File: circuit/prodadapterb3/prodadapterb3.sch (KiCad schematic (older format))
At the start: 8 parts, among them J1 Conn_02x20_Odd_Even, J2 Conn_02x05_Odd_Even, J3 Conn_01x02, J4 Conn_02x20_Odd_Even, U1 24LC128

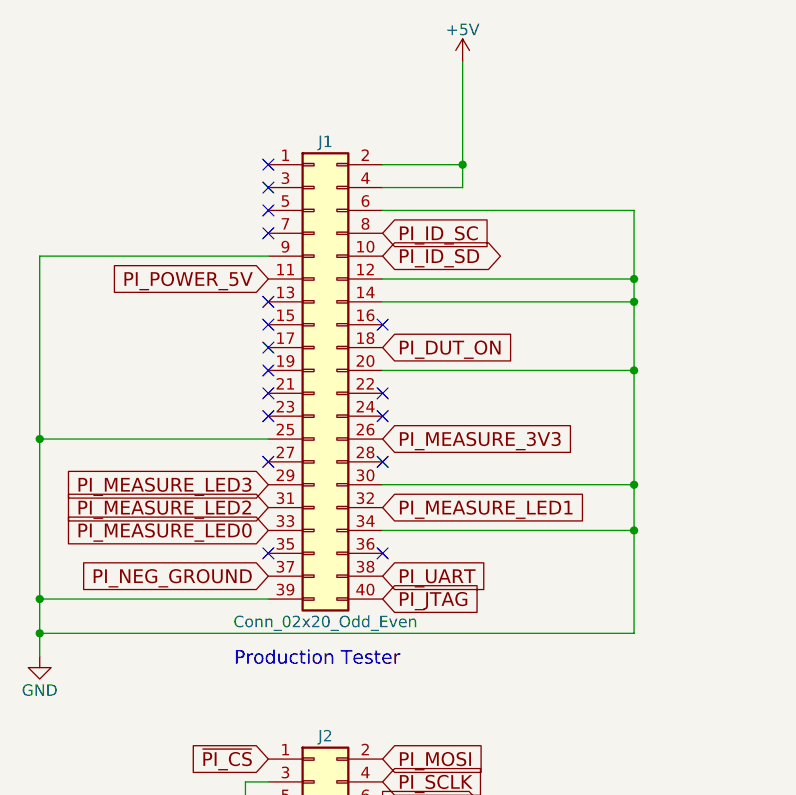
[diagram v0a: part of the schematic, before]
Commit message: prodadapterb3: move resistors out of the way and connect up 3v3 line
Signed-off-by: Gavan Fantom <gavan.fantom@unipart.io>
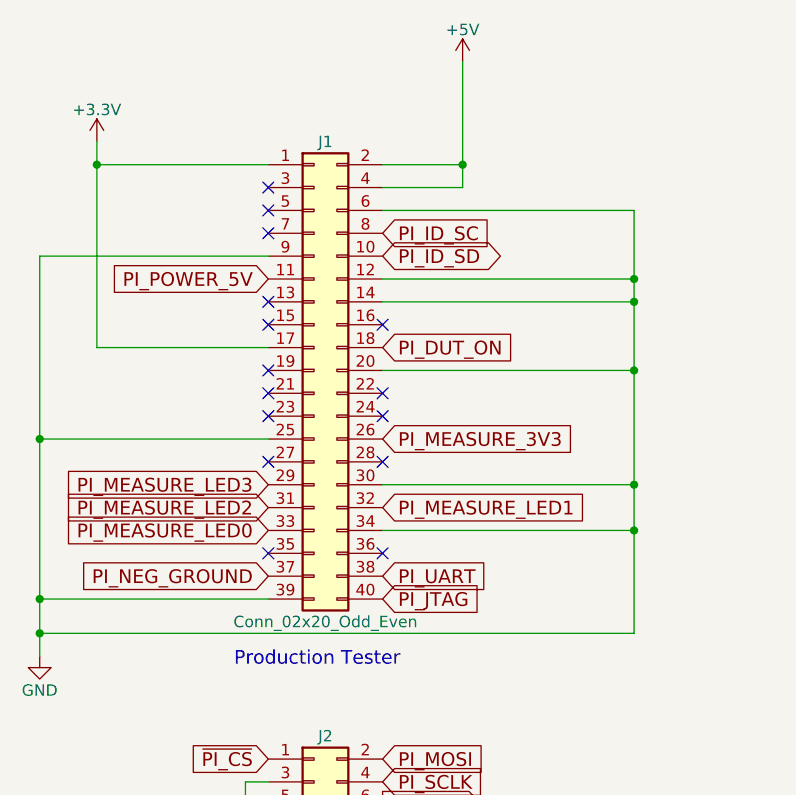
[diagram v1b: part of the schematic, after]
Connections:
- net +3V3: now also J1.1 (Pin_1), J1.17 (Pin_17)
- no-connect marks 27 -> 25
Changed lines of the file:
@@
 $EndComp
 Wire Wire Line
-	2900 3800 1900 3800
+	1900 3800 2900 3800
 Wire Wire Line
 	1900 2300 1900 4050
@@
 Connection ~ 1900 3100
 Wire Wire Line
-	1900 3950 4500 3950
+	4500 3950 1900 3950
 Wire Wire Line
-	4500 3950 4500 2100
+	4500 2100 4500 3950
 Wire Wire Line
 	4500 2100 3400 2100
@@
 	1    0    0    -1
 $EndComp
-NoConn ~ 2900 1900
 NoConn ~ 2900 2000
 NoConn ~ 2900 2100
@@
 NoConn ~ 2900 2600
 NoConn ~ 2900 2500
-NoConn ~ 2900 2700
 NoConn ~ 6500 2200
 NoConn ~ 7000 2200
@@
 Connection ~ 6250 1900
 Connection ~ 7100 1900
+Wire Wire Line
+	2150 2700 2900 2700
+Wire Wire Line
+	2150 1800 2150 2700
+Wire Wire Line
+	2150 1900 2900 1900
+Connection ~ 2150 1900
+$Comp
+L +3.3V #PWR011
+U 1 1 5DC1768B
+P 2150 1800
+F 0 "#PWR011" H 2150 1650 50  0001 C CNN
+F 1 "+3.3V" H 2150 1940 50  0000 C CNN
+F 2 "" H 2150 1800 50  0001 C CNN
+F 3 "" H 2150 1800 50  0001 C CNN
+	1    2150 1800
+	1    0    0    -1
+$EndComp
 $EndSCHEMATC

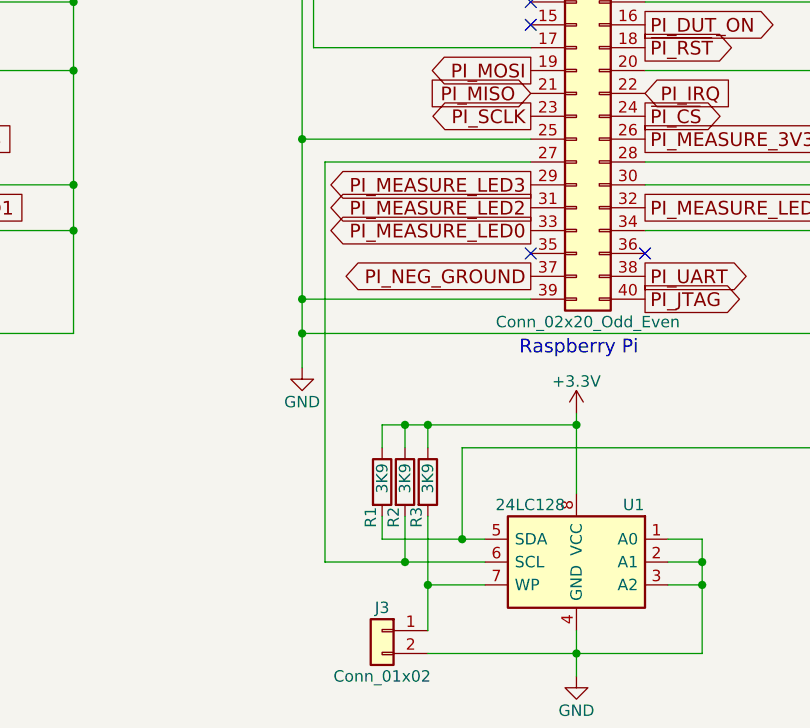
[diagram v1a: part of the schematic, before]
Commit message: prodadapterb3: Swap SCA and SCL (oops!)
Signed-off-by: Gavan Fantom <gavan.fantom@unipart.io>
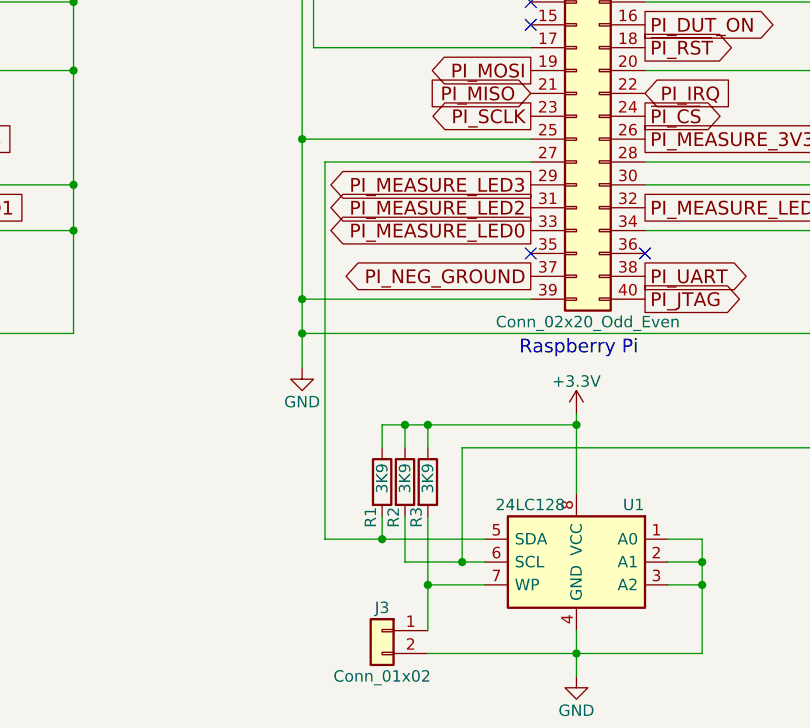
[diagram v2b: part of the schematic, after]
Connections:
- net at R2.2, U1.6 (SCL): now also J4.28 (Pin_28); no longer J4.27 (Pin_27)
- net at R1.2, U1.5 (SDA): now also J4.27 (Pin_27); no longer J4.28 (Pin_28)
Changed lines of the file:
@@
 Connection ~ 6050 4350
 Wire Wire Line
-	5950 4750 5950 4950
-Wire Wire Line
-	5600 4950 6300 4950
-Wire Wire Line
-	5850 4750 5850 4850
-Wire Wire Line
-	5850 4850 6300 4850
+	5600 4850 6300 4850
 Wire Wire Line
 	5950 4450 5950 4350
@@
 	5850 4450 5850 4350
 Wire Wire Line
-	5600 4950 5600 3200
-Wire Wire Line
 	5600 3200 6500 3200
-Connection ~ 5950 4950
-Wire Wire Line
-	6200 4850 6200 4450
 Wire Wire Line
 	6200 4450 8000 4450
@@
 Wire Wire Line
 	8000 3200 7000 3200
-Connection ~ 6200 4850
 Wire Wire Line
 	7100 4850 7250 4850
@@
 	1    0    0    -1
 $EndComp
+Wire Wire Line
+	6200 4450 6200 4950
+Connection ~ 6200 4950
+Wire Wire Line
+	5600 3200 5600 4850
+Wire Wire Line
+	5950 4750 5950 4950
+Wire Wire Line
+	5850 4750 5850 4850
+Connection ~ 5850 4850
+Wire Wire Line
+	5950 4950 6300 4950
 $EndSCHEMATC
